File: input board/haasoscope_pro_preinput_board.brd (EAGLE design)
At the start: 75 x 50 mm, 31 parts, among them J1 MOLEX_BNC_73100-0105, J4 8pin, K1 AQY21SOP, K2 G6K-2F-RF-DC3, K3 G6K-2F-RF-DC3, Q1 S8050, Q2 S8050

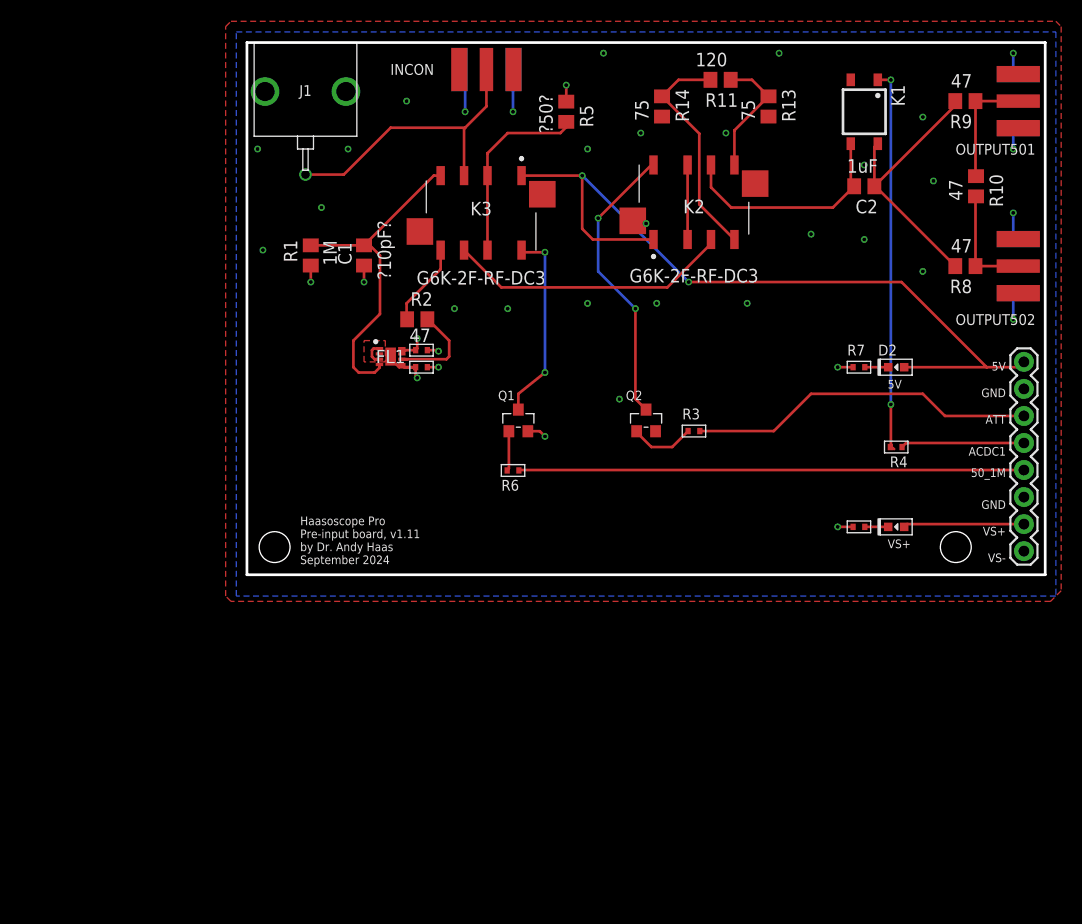
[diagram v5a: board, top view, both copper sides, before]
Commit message: add relay for splitter add ethernet jack for testing lvds add connector and trace test lines
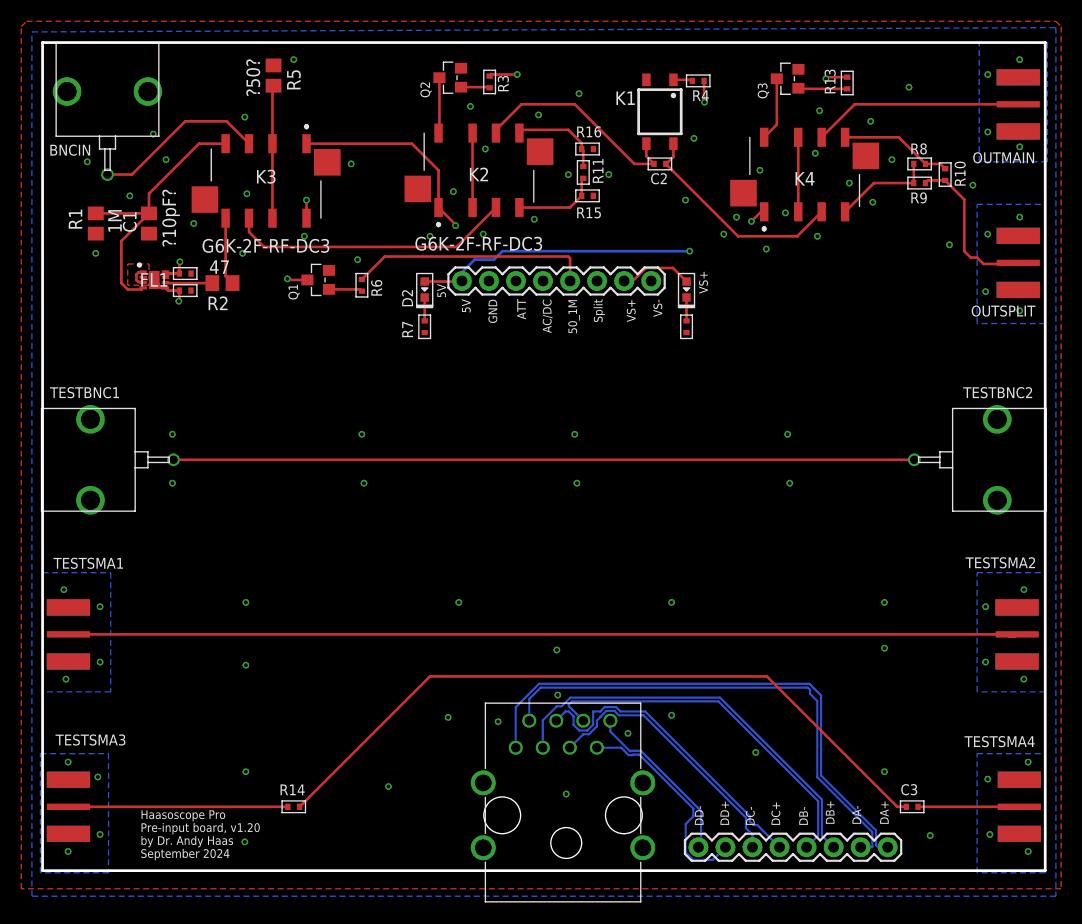
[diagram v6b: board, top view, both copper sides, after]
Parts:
- removed INCON: in, adafruit:SMA_EDGELAUNCH
- removed J1: MOLEX_BNC_73100-0105, connector:MOLEX-BNC-73100-0105
- removed OUTPUT501, OUTPUT502: out50, adafruit:SMA_EDGELAUNCH
- added BNCIN, TESTBNC1, TESTBNC2: MOLEX_BNC_73100-0105, connector:MOLEX-BNC-73100-0105
- added C3: 1uF, MF_Passives:C0402
- added J2: 8pin, SparkFun-Connectors:1X08
- added K4: G6K-2F-RF-DC3, G6K-2F-RF-DC3:G6K2FRFDC3
- added OUTMAIN, OUTSPLIT, TESTSMA1, TESTSMA2, TESTSMA3, TESTSMA4: out50, adafruit:SMA_EDGELAUNCH
- added Q3: S8050, Seeed-Transistor:SOT-23
- added R15, R16: 75, MF_Passives:R0402
- added U$1: RJ45-CONNECTOR-SHIELDED, FlashPCB_Connectors:RJ45_THT_RA_AMPH-FRJAE448
- C2: device resistor:C0805 -> MF_Passives:C0402
- R10, R11, R8, R9: device resistor:R0805 -> MF_Passives:R0402
- R13: value 75 -> 1k; device resistor:R0805 -> MF_Passives:R0402
- R14: value 75 -> 0; device resistor:R0805 -> MF_Passives:R0402
- moved R14 74.3 mm to (14.4, -21.8), turned to 180 degrees
- moved J4 53.3 mm to (30.2, 27.6), turned to 0 degrees
- moved D2 44.9 mm to (26.7, 26.8), turned to 90 degrees
- moved R7 41.0 mm to (26.7, 23.3), turned to 90 degrees
- moved R4 39.1 mm to (52.4, 46.4)
- moved R3 38.0 mm to (32.8, 46.3), turned to 90 degrees
- moved Q2 37.1 mm to (29.1, 46.7), turned to 90 degrees
- moved D1 29.8 mm to (51.3, 26.8), turned to 90 degrees
- moved R5 27.7 mm to (12.5, 46.9)
- moved R12 24.8 mm to (51.3, 23.3), turned to 90 degrees
- moved C11 23.3 mm to (4.20, 28.3)
- moved C12 23.3 mm to (4.20, 26.7)
- moved FL1 23.3 mm to (1.30, 27.7)
- moved Q1 23.0 mm to (16.7, 27.7), turned to 90 degrees
- moved R6 22.5 mm to (20.8, 27.2), turned to 90 degrees
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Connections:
- net 50_1M renamed 50_1M_CONTROL
- net ACDC1 renamed ACDC_CONTROL
- net ATT renamed ATT_CONTROL
- new net COIL3-: K4.8, Q3.3
- new net DA_N: J2.2, U$1.P$2
- new net DA_P: J2.1, U$1.P$1
- new net DB_N: J2.4, U$1.P$6
- new net DB_P: J2.3, U$1.P$3
- new net DC_N: J2.6, U$1.P$5
- new net DC_P: J2.5, U$1.P$4
- new net DD_N: J2.8, U$1.P$8
- new net DD_P: J2.7, U$1.P$7
- new net N$12: C3.P$1, R14.P$1
- new net N$13: C3.P$2, TESTSMA4.P
- new net N$3: Q3.1, R13.P$1
- new net NOSPLIT: K4.2, K4.7
- new net OUTMAIN: K4.6, OUTMAIN.P
- new net OUTPATHACDC: C2.P$2, K1.4, K4.3
- new net OUTSPLIT: OUTSPLIT.P, R10.P$2, R9.P$2
- new net SPLIT: K4.4, R8.P$1, R9.P$1
- new net SPLITOUT: K4.5, R10.P$1, R8.P$2
- new net SPLIT_CONTROL: J4.6, R13.P$2
- net 5V: now also K4.1
- net FILTIN: now also R11.P$1, R15.P$1; no longer R11.2, R14.1
- net FILTOUT: now also R11.P$2, R16.P$1; no longer R11.1, R13.1
- net GND: now also BNCIN.GND1, BNCIN.GND2, K4.MP1, K4.MP2, OUTMAIN.GND@1, OUTMAIN.GND@2, OUTMAIN.GND@3, OUTMAIN.GND@4, OUTSPLIT.GND@1, OUTSPLIT.GND@2, OUTSPLIT.GND@3, OUTSPLIT.GND@4, Q3.2, R15.P$2, R16.P$2, TESTBNC1.GND1, TESTBNC1.GND2, TESTBNC2.GND1, TESTBNC2.GND2, TESTSMA1.GND@1, TESTSMA1.GND@2, TESTSMA1.GND@3, TESTSMA1.GND@4, TESTSMA2.GND@1, TESTSMA2.GND@2, TESTSMA2.GND@3, TESTSMA2.GND@4, TESTSMA3.GND@1, TESTSMA3.GND@2, TESTSMA3.GND@3, TESTSMA3.GND@4, TESTSMA4.GND@1, TESTSMA4.GND@2, TESTSMA4.GND@3, TESTSMA4.GND@4, U$1.S$1, U$1.S$2, U$1.S$3, U$1.S$4; no longer INCON.GND@1, INCON.GND@2, INCON.GND@3, INCON.GND@4, J1.GND1, J1.GND2, J4.6, OUTPUT501.GND@1, OUTPUT501.GND@2, OUTPUT501.GND@3, OUTPUT501.GND@4, OUTPUT502.GND@1, OUTPUT502.GND@2, OUTPUT502.GND@3, OUTPUT502.GND@4, R13.2, R14.2
- net INPATH: now also BNCIN.SIGNAL; no longer INCON.P, J1.SIGNAL
- net N$10: now also R14.P$2, TESTSMA3.P; no longer OUTPUT501.P, R10.1, R9.1
- net N$8: now also TESTBNC1.SIGNAL, TESTBNC2.SIGNAL; no longer C2.1, K1.4, R8.2, R9.2
- net N$9: now also TESTSMA1.P, TESTSMA2.P; no longer OUTPUT502.P, R10.2, R8.1
- net OUTPATHFILT: now also C2.P$1; no longer C2.2
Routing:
- net N$9: track 11.1 -> 89.3 mm
- net N$12: track 0.00 -> 67.1 mm
- net DA_P: track 0.00 -> 51.2 mm
- net DA_N: track 0.00 -> 47.2 mm
- net N$8: track 26.4 -> 69.6 mm
- net DB_P: track 0.00 -> 38.6 mm
- net N$11: track 36.4 -> 1.82 mm, vias 2 -> 0
- net DB_N: track 0.00 -> 34.3 mm
- net SPLIT_CONTROL: track 0.00 -> 32.0 mm, vias 0 -> 1
- net DC_P: track 0.00 -> 29.9 mm
- net GND: track 29.6 -> 0.00 mm, vias 37 -> 91
- net DC_N: track 0.00 -> 25.5 mm
- net 50_1M_CONTROL: track 47.5 -> 22.7 mm
- net COIL2-: track 27.1 -> 5.23 mm, vias 2 -> 0
- net OUTPATHACDC: track 0.00 -> 20.6 mm
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- added copper zone on layer 15, net GND
- added copper zone on layer 16, net GND
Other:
- board size 75 x 50 mm -> 94.2 x 77.8 mm
- board text added: "AC/DC"
- board text added: "DA+"
- board text added: "DA-"
- board text added: "DB+"
- board text added: "DB-"
- board text added: "DC+"
- board text added: "DC-"
- board text added: "DD+"
- board text added: "DD-"
- board text added: "Haasoscope Pro Pre-input board, v1.20 by Dr. Andy Haas September 2024"
- board text added: "Split"
- board text removed: "ACDC1"
- board text removed: "Haasoscope Pro Pre-input board, v1.11 by Dr. Andy Haas September 2024"

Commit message: add usb A port for powering probe
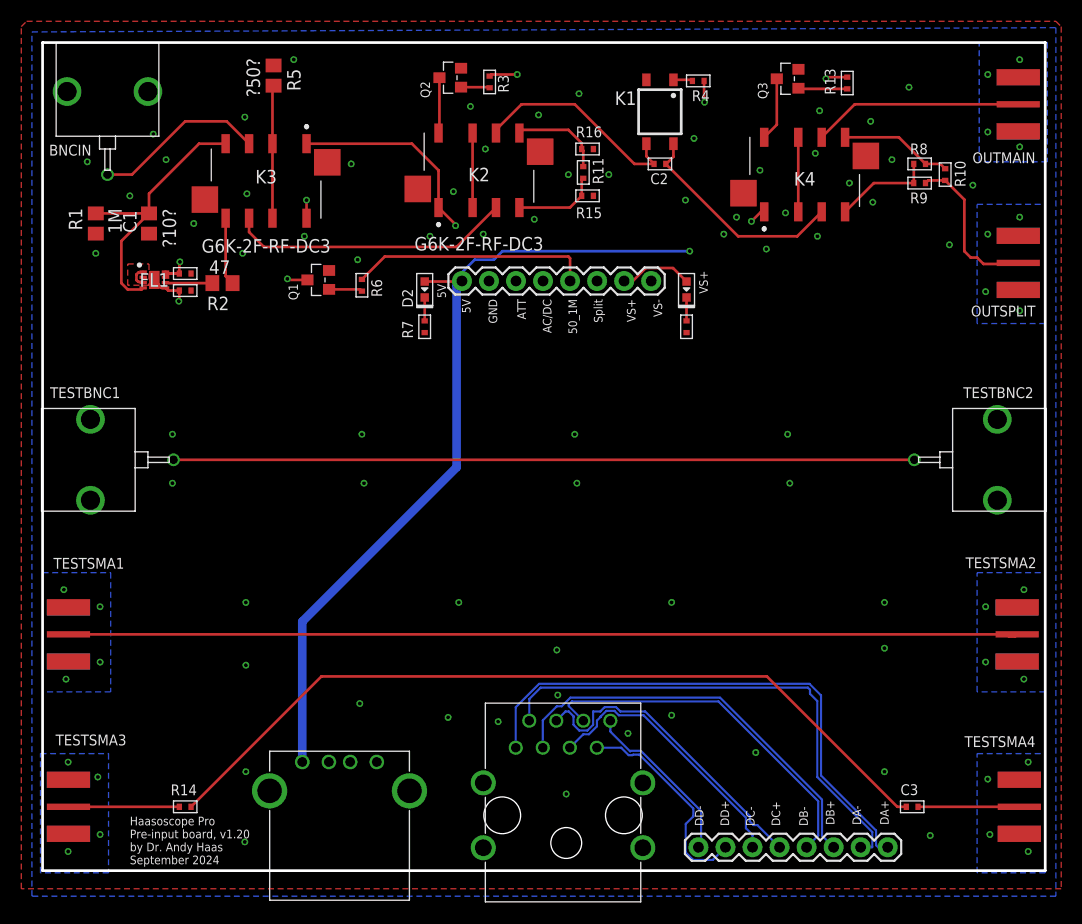
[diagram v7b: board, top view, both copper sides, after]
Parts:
- added J1: test1, FlashPCB_Connectors:USB-2.0-A-THT-RA-TE_AMP-292303-1
- C1: value ?10pF? -> ?10?
- moved R14 10.2 mm to (4.20, -21.8)
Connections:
- net 5V: now also J1.P$1
- net GND: now also J1.P$4
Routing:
- net 5V: track 59.8 -> 111.3 mm
- net N$12: track 67.1 -> 77.3 mm
- net N$10: track 20.6 -> 10.4 mm
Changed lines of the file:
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@@
 <wire x1="85" y1="50" x2="-9.2" y2="50" width="0.254" layer="20"/>
 <hole x="40" y="-25.2" drill="2.9"/>
-<text x="0" y="-26.6" size="0.8128" layer="21">Haasoscope Pro
+<text x="-1" y="-27.2" size="0.8128" layer="21">Haasoscope Pro
 Pre-input board, v1.20
 by Dr. Andy Haas
@@
 <attribute name="VALUE" x="-1.76" y="32.065" size="1.27" layer="21" rot="R90"/>
 </element>
-<element name="C1" library="resistor" library_urn="urn:adsk.eagle:library:348" package="C0805" package3d_urn="urn:adsk.eagle:package:23617/2" value="?10pF?" x="0.8" y="33" smashed="yes" rot="R90">
+<element name="C1" library="resistor" library_urn="urn:adsk.eagle:library:348" package="C0805" package3d_urn="urn:adsk.eagle:package:23617/2" value="?10?" x="0.8" y="33" smashed="yes" rot="R90">
 <attribute name="NAME" x="-0.37" y="32.13" size="1.27" layer="25" rot="R90"/>
 <attribute name="VALUE" x="3.34" y="30.73" size="1.27" layer="21" rot="R90"/>
@@
 <attribute name="VOLTAGE" value="" x="72.5" y="-21.8" size="1.778" layer="27" display="off"/>
 </element>
-<element name="R14" library="MF_Passives" package="R0402" value="0" x="14.4" y="-21.8" smashed="yes" rot="R180">
-<attribute name="HOUSEPART" value="" x="14.4" y="-21.8" size="1.778" layer="27" rot="R180" display="off"/>
-<attribute name="MPN" value="" x="14.4" y="-21.8" size="1.778" layer="27" rot="R180" display="off"/>
-<attribute name="NAME" x="15.5" y="-19.7" size="1.016" layer="25" font="vector" ratio="16" rot="R180"/>
-<attribute name="POPULATE" value="1" x="14.4" y="-21.8" size="1.778" layer="27" rot="R180" display="off"/>
-<attribute name="TOLERANCE" value="" x="14.4" y="-21.8" size="1.778" layer="27" rot="R180" display="off"/>
-<attribute name="URL" value="" x="14.4" y="-21.8" size="1.778" layer="27" rot="R180" display="off"/>
-<attribute name="VOLTAGE" value="" x="14.4" y="-21.8" size="1.778" layer="27" rot="R180" display="off"/>
-<attribute name="WATTAGE" value="" x="14.4" y="-21.8" size="1.778" layer="27" rot="R180" display="off"/>
+<element name="R14" library="MF_Passives" package="R0402" value="0" x="4.2" y="-21.8" smashed="yes" rot="R180">
+<attribute name="HOUSEPART" value="" x="4.2" y="-21.8" size="1.778" layer="27" rot="R180" display="off"/>
+<attribute name="MPN" value="" x="4.2" y="-21.8" size="1.778" layer="27" rot="R180" display="off"/>
+<attribute name="NAME" x="5.3" y="-19.7" size="1.016" layer="25" font="vector" ratio="16" rot="R180"/>
+<attribute name="POPULATE" value="1" x="4.2" y="-21.8" size="1.778" layer="27" rot="R180" display="off"/>
+<attribute name="TOLERANCE" value="" x="4.2" y="-21.8" size="1.778" layer="27" rot="R180" display="off"/>
+<attribute name="URL" value="" x="4.2" y="-21.8" size="1.778" layer="27" rot="R180" display="off"/>
+<attribute name="VOLTAGE" value="" x="4.2" y="-21.8" size="1.778" layer="27" rot="R180" display="off"/>
+<attribute name="WATTAGE" value="" x="4.2" y="-21.8" size="1.778" layer="27" rot="R180" display="off"/>
 </element>
 <element name="U$1" library="FlashPCB_Connectors" package="RJ45_THT_RA_AMPH-FRJAE448" value="RJ45-CONNECTOR-SHIELDED" x="39.7" y="-22.6" smashed="yes">
@@
 <element name="J2" library="SparkFun-Connectors" library_urn="urn:adsk.eagle:library:513" package="1X08" package3d_urn="urn:adsk.eagle:package:38138/1" value="8pin" x="70.2" y="-25.6" smashed="yes" rot="R180">
 <attribute name="PROD_ID" value="CONN-08438" x="70.2" y="-25.6" size="1.778" layer="27" rot="R180" display="off"/>
+</element>
+<element name="J1" library="FlashPCB_Connectors" package="USB-2.0-A-THT-RA-TE_AMP-292303-1" value="test1" x="18.7" y="-20.3" smashed="yes">
+<attribute name="VALUE" x="12.35" y="-15.855" size="0.8128" layer="27" font="vector"/>
 </element>
 </elements>
@@
 <via x="74.2" y="-24.5" extent="1-16" drill="0.35"/>
 <via x="57.8" y="-16.7" extent="1-16" drill="0.35"/>
-<via x="23.3" y="-19.9" extent="1-16" drill="0.35"/>
+<via x="20.6" y="-12.1" extent="1-16" drill="0.35"/>
 <via x="9.8" y="-25.1" extent="1-16" drill="0.35"/>
 <contactref element="U$1" pad="S$3"/>
@@
 <via x="45.8" y="-14.9" extent="1-16" drill="0.35"/>
 <via x="40" y="-20.6" extent="1-16" drill="0.35"/>
+<contactref element="J1" pad="P$4"/>
 </signal>
 <signal name="VS+" airwireshidden="yes">
@@
 <wire x1="33.2" y1="29.6" x2="31.4" y2="29.6" width="0.254" layer="16"/>
 <wire x1="31.4" y1="29.6" x2="30.2" y2="28.4" width="0.254" layer="16"/>
-<wire x1="30.2" y1="28.4" x2="30.2" y2="27.6" width="0.254" layer="16"/>
+<wire x1="30.2" y1="28.4" x2="30.2" y2="27.7" width="0.254" layer="16"/>
+<wire x1="30.2" y1="27.7" x2="30.2" y2="27.6" width="0.254" layer="16"/>
 <wire x1="54.6" y1="30.4" x2="51.6" y2="30.4" width="0.254" layer="15"/>
 <wire x1="34" y1="30.4" x2="33.2" y2="29.6" width="0.254" layer="16"/>
+<contactref element="J1" pad="P$1"/>
+<wire x1="15.2" y1="-17.59" x2="15.2" y2="-4.4" width="0.8128" layer="16"/>
+<wire x1="29.7" y1="27.2" x2="30.2" y2="27.7" width="0.8128" layer="16"/>
+<wire x1="15.2" y1="-4.4" x2="29.7" y2="10.1" width="0.8128" layer="16"/>
+<wire x1="29.7" y1="10.1" x2="29.7" y2="27.2" width="0.8128" layer="16"/>
 </signal>
 <signal name="COIL1-">
@@
 <contactref element="TESTSMA3" pad="P"/>
 <contactref element="R14" pad="P$2"/>
-<wire x1="-6.768" y1="-21.8" x2="13.85" y2="-21.8" width="0.254" layer="1"/>
+<wire x1="-6.768" y1="-21.8" x2="3.65" y2="-21.8" width="0.254" layer="1"/>
 </signal>
 <signal name="N$12">
 <contactref element="R14" pad="P$1"/>
 <contactref element="C3" pad="P$1"/>
-<wire x1="14.95" y1="-21.8" x2="27.2" y2="-9.55" width="0.254" layer="1"/>
-<wire x1="27.2" y1="-9.55" x2="58.85" y2="-9.55" width="0.254" layer="1"/>
+<wire x1="4.75" y1="-21.8" x2="17" y2="-9.55" width="0.254" layer="1"/>
+<wire x1="17" y1="-9.55" x2="58.85" y2="-9.55" width="0.254" layer="1"/>
 <wire x1="58.85" y1="-9.55" x2="71.1" y2="-21.8" width="0.254" layer="1"/>
 <wire x1="71.1" y1="-21.8" x2="71.95" y2="-21.8" width="0.254" layer="1"/>

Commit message: specify rf dc blocking cap
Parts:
- C2: value 1uF -> RF_1uF
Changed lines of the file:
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@@
 <drawing>
 <settings>
-<setting alwaysvectorfont="yes"/>
+<setting alwaysvectorfont="no"/>
 <setting verticaltext="up"/>
 </settings>
@@
 <attribute name="WATTAGE" value="" x="75.6" y="37.6" size="1.778" layer="27" rot="R270" display="off"/>
 </element>
-<element name="C2" library="MF_Passives" package="C0402" value="1uF" x="48.8" y="38.6" smashed="yes">
+<element name="C2" library="MF_Passives" package="C0402" value="RF_1uF" x="48.8" y="38.6" smashed="yes">
 <attribute name="DIELECTRIC" value="" x="48.8" y="38.6" size="1.778" layer="27" display="off"/>
 <attribute name="HOUSEPART" value="" x="48.8" y="38.6" size="1.778" layer="27" display="off"/>
+<attribute name="LCSC" value="C52923" x="48.8" y="38.6" size="1.778" layer="27" display="off"/>
 <attribute name="MPN" value="" x="48.8" y="38.6" size="1.778" layer="27" display="off"/>
 <attribute name="NAME" x="47.9" y="36.7" size="1.016" layer="25" font="vector" ratio="16"/>
@@
 <signal name="GND" airwireshidden="yes">
 <polygon width="0.254" layer="2">
-<vertex x="88" y="54.5"/>
 <vertex x="88" y="54.5"/>
 <vertex x="88" y="-31"/>
@@
 <vertex x="-10.2" y="51"/>
 <vertex x="86" y="51.4"/>
-<vertex x="86" y="51.4"/>
 <vertex x="86" y="-30.2"/>
 <vertex x="-10.2" y="-30.2"/>
@@
 <vertex x="-12.2" y="53.5"/>
 <vertex x="87" y="53.9"/>
-<vertex x="87" y="53.9"/>
 <vertex x="87" y="-28.8"/>
